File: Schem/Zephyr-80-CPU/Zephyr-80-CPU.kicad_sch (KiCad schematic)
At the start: 2 parts

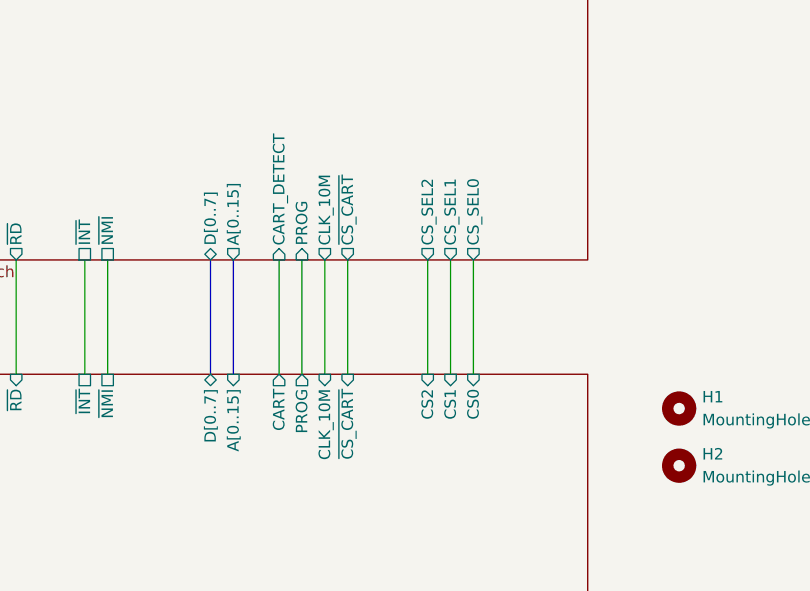
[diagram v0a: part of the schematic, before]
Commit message: Moved to the DIN Connector
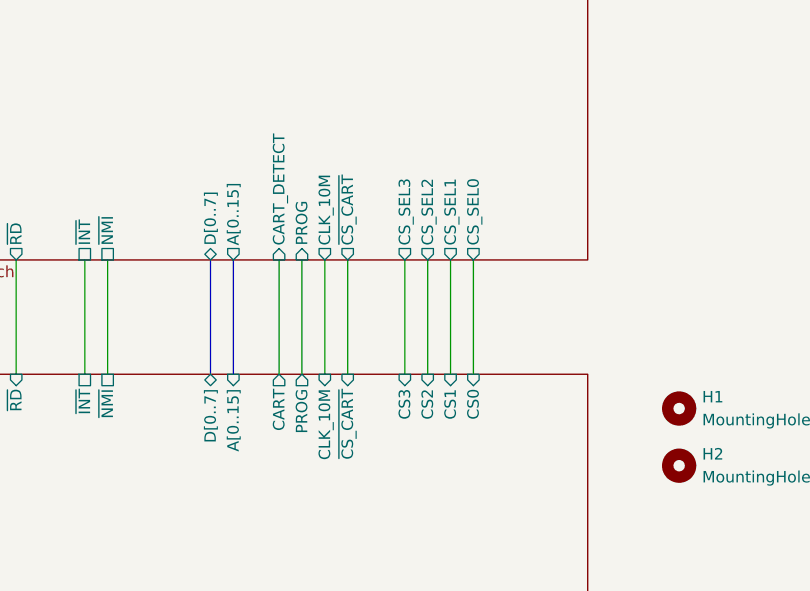
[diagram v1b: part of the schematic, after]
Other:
- sheet CPU and Address Decoding ports: added CS_SEL3; removed none
- sheet pBITz Bus Interface ports: added CS3; removed none
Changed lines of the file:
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@@
+	(wire
+		(pts
+			(xy 104.14 96.52) (xy 104.14 109.22)
+		)
+		(stroke
+			(width 0)
+			(type default)
+		)
+	)
 	(wire
 		(pts
@@
 			)
 		)
+		(pin "CS_SEL3" output
+			(at 104.14 96.52 270)
+			(effects
+				(font
+					(size 1.27 1.27)
+				)
+				(justify left)
+			)
+		)
 		(instances
 			(project "Zephyr-80-CPU"
@@
 			(effects
 				(font
+					(size 1.27 1.27)
+				)
+				(justify right)
+			)
+		)
+		(pin "CS3" input
+			(at 104.14 109.22 90)
+			(effects
+				(font
